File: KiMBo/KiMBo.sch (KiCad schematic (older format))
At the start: 74 parts, among them CON1 μSD, P1 BED, P10 CONN_01X02, P11 Serial, P12 μUSB, P13 USB_Type_A, P14 Ethernet, P15 JTAG, P16 CONN_01X04, P17 CONN_01X04, P18 CONN_01X04, P19 CONN_01X04, P2 ADC, P20 CONN_01X04, P21 CONN_01X04, P22 CONN_01X04, P23 CONN_01X04, P24 CONN_01X04, P25 BED_HEAT, P26 E_HEAT, P27 H_HEAT, P28 DOCK0_HEAT, P29 DOCK1_HEAT, P3 CONN_01X07, P30 E_FAN, P31 H_FAN, P32 PWM, P33 CASE_FAN, P34 HS_FAN, P4 CONN_01X07, P5 CONN_01X07, P6 CONN_01X07, P7 CONN_01X02, P8 CONN_01X02, P9 CONN_01X02, U1 MAX3370, X1 10118241-001RLF

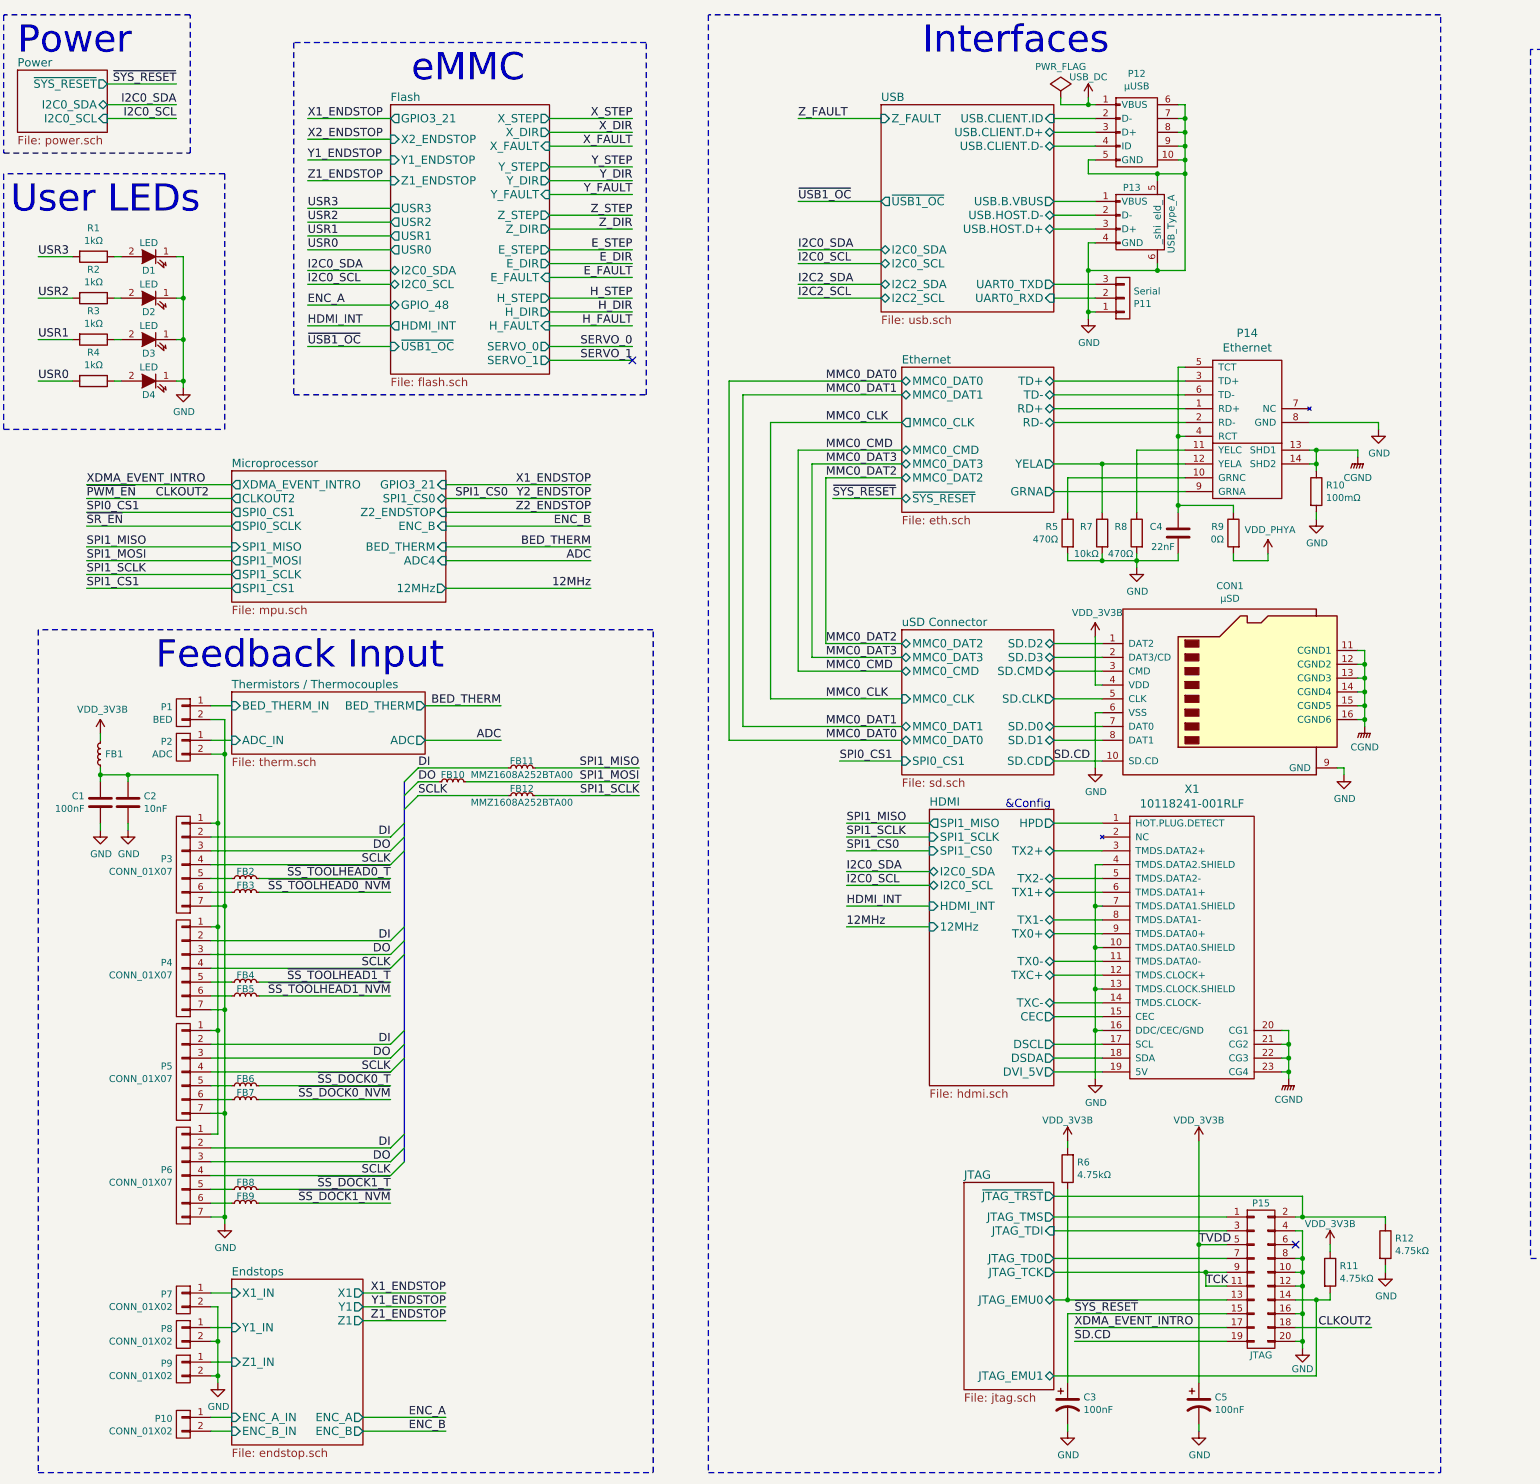
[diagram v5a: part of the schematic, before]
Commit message: Replace most electrolytic cap symbols symbols with the standard, non-polarized (ceramic) cap symbol
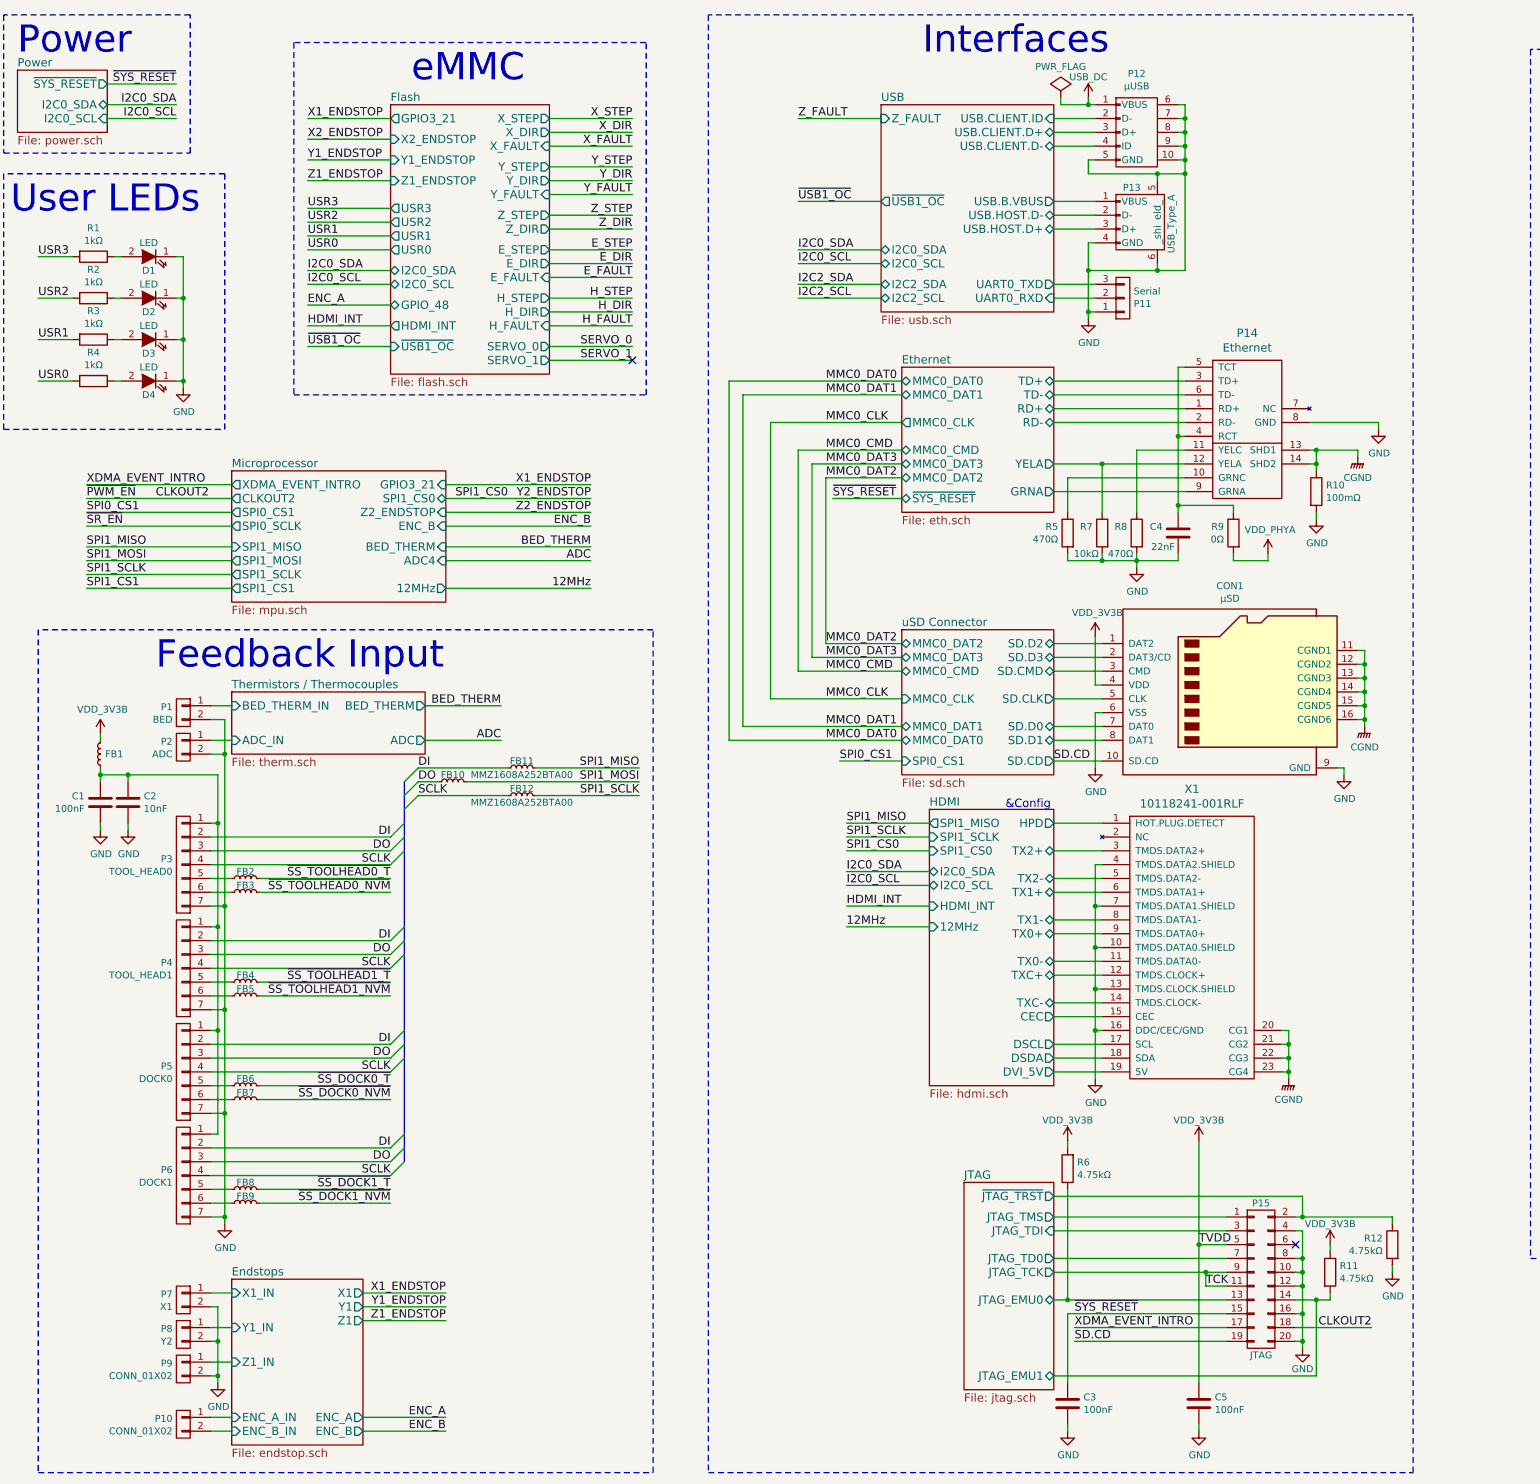
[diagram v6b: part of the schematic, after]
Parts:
- removed C3, C5: 100nF, symbol CP1
- added C3, C5: 100nF, symbol C
- C1, C2: footprint (none) -> Capacitors_SMD:C_0603
- P3: value CONN_01X07 -> TOOL_HEAD0
- P4: value CONN_01X07 -> TOOL_HEAD1
- P5: value CONN_01X07 -> DOCK0
- P6: value CONN_01X07 -> DOCK1
- P7: value CONN_01X02 -> X1
- P8: value CONN_01X02 -> Y2
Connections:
- net GND: now also C3.2, C5.2
- net VDD_3V3B: now also C5.1
- net ~SYS_RESET: now also C3.1
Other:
- moved on the sheet: R12
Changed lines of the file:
@@
 TVDD
-$Comp
-L CP1 C5
-U 1 1 58FEA321
-P 9250 10600
-F 0 "C5" H 9365 10646 50  0000 L CNN
-F 1 "100nF" H 9365 10555 50  0000 L CNN
-F 2 "" H 9250 10600 50  0001 C CNN
-F 3 "" H 9250 10600 50  0000 C CNN
-	1    9250 10600
-	1    0    0    -1
-$EndComp
 $Comp
 L GND #PWR011
@@
 $EndComp
 $Comp
-L CP1 C3
-U 1 1 58FEA335
-P 8300 10600
-F 0 "C3" H 8415 10646 50  0000 L CNN
-F 1 "100nF" H 8415 10555 50  0000 L CNN
-F 2 "" H 8300 10600 50  0001 C CNN
-F 3 "" H 8300 10600 50  0000 C CNN
-	1    8300 10600
-	1    0    0    -1
-$EndComp
-$Comp
 L GND #PWR012
 U 1 1 58FEA33C
@@
 L GND #PWR014
 U 1 1 58FEA383
-P 10600 9650
-F 0 "#PWR014" H 10600 9400 50  0001 C CNN
-F 1 "GND" H 10605 9477 50  0000 C CNN
-F 2 "" H 10600 9650 50  0000 C CNN
-F 3 "" H 10600 9650 50  0000 C CNN
-	1    10600 9650
+P 10650 9650
+F 0 "#PWR014" H 10650 9400 50  0001 C CNN
+F 1 "GND" H 10655 9477 50  0000 C CNN
+F 2 "" H 10650 9650 50  0000 C CNN
+F 3 "" H 10650 9650 50  0000 C CNN
+	1    10650 9650
 	1    0    0    -1
 $EndComp
@@
 L R R12
 U 1 1 58FEA389
-P 10600 9450
-F 0 "R12" H 10670 9496 50  0000 L CNN
-F 1 "4.75kΩ" H 10670 9405 50  0000 L CNN
-F 2 "" V 10530 9450 50  0001 C CNN
-F 3 "" H 10600 9450 50  0000 C CNN
-	1    10600 9450
-	1    0    0    -1
+P 10650 9450
+F 0 "R12" H 10720 9496 50  0000 L CNN
+F 1 "4.75kΩ" H 10720 9405 50  0000 L CNN
+F 2 "" V 10580 9450 50  0001 C CNN
+F 3 "" H 10650 9450 50  0000 C CNN
+	1    10650 9450
+	-1   0    0    -1
 $EndComp
 $Comp
@@
 P 1900 9850
 F 0 "P7" H 1978 9891 50  0000 L CNN
-F 1 "CONN_01X02" H 1978 9800 50  0000 L CNN
+F 1 "X1" H 1978 9800 50  0000 L CNN
 F 2 "" H 1900 9850 50  0001 C CNN
 F 3 "" H 1900 9850 50  0000 C CNN
@@
 P 1900 10100
 F 0 "P8" H 1978 10141 50  0000 L CNN
-F 1 "CONN_01X02" H 1978 10050 50  0000 L CNN
+F 1 "Y2" H 1978 10050 50  0000 L CNN
 F 2 "" H 1900 10100 50  0001 C CNN
 F 3 "" H 1900 10100 50  0000 C CNN
@@
 P 1900 6700
 F 0 "P3" H 1978 6741 50  0000 L CNN
-F 1 "CONN_01X07" H 1978 6650 50  0000 L CNN
+F 1 "TOOL_HEAD0" H 1978 6650 50  0000 L CNN
 F 2 "" H 1900 6700 50  0001 C CNN
 F 3 "" H 1900 6700 50  0000 C CNN
@@
 P 1900 8200
 F 0 "P5" H 1978 8241 50  0000 L CNN
-F 1 "CONN_01X07" H 1978 8150 50  0000 L CNN
+F 1 "DOCK0" H 1978 8150 50  0000 L CNN
 F 2 "" H 1900 8200 50  0001 C CNN
 F 3 "" H 1900 8200 50  0000 C CNN
@@
 P 1900 8950
 F 0 "P6" H 1978 8991 50  0000 L CNN
-F 1 "CONN_01X07" H 1978 8900 50  0000 L CNN
+F 1 "DOCK1" H 1978 8900 50  0000 L CNN
 F 2 "" H 1900 8950 50  0001 C CNN
 F 3 "" H 1900 8950 50  0000 C CNN
@@
 P 1900 7450
 F 0 "P4" H 1978 7491 50  0000 L CNN
-F 1 "CONN_01X07" H 1978 7400 50  0000 L CNN
+F 1 "TOOL_HEAD1" H 1978 7400 50  0000 L CNN
 F 2 "" H 1900 7450 50  0001 C CNN
 F 3 "" H 1900 7450 50  0000 C CNN
@@
 F 0 "C2" H 1614 6296 50  0000 L CNN
 F 1 "10nF" H 1614 6205 50  0000 L CNN
-F 2 "" H 1538 6100 50  0001 C CNN
+F 2 "Capacitors_SMD:C_0603" H 1538 6100 50  0001 C CNN
 F 3 "" H 1500 6250 50  0000 C CNN
 	1    1500 6250
@@
 F 0 "C1" H 1415 6296 50  0000 L CNN
 F 1 "100nF" H 1415 6205 50  0000 L CNN
-F 2 "" H 1338 6100 50  0001 C CNN
+F 2 "Capacitors_SMD:C_0603" H 1338 6100 50  0001 C CNN
 F 3 "" H 1300 6250 50  0000 C CNN
 	1    1300 6250
@@
 	9450 10150 8350 10150
 Wire Wire Line
-	9950 9250 10600 9250
+	9950 9250 10650 9250
 Wire Wire Line
 	9450 9750 9300 9750
@@
 	10200 9850 10200 9800
 Wire Wire Line
-	10600 9250 10600 9300
-Wire Wire Line
-	10600 9650 10600 9600
+	10650 9250 10650 9300
+Wire Wire Line
+	10650 9650 10650 9600
 Wire Wire Line
 	8500 6700 8500 8250
@@
 	5700 550  5700 11100
 Wire Notes Line
-	5700 11100 11000 11100
-Wire Notes Line
-	11000 11100 11000 550
-Wire Notes Line
-	11000 550  5700 550
+	5700 11100 10800 11100
+Wire Notes Line
+	10800 11100 10800 550
+Wire Notes Line
+	10800 550  5700 550
 Wire Notes Line
 	850  11100 5300 11100
@@
 Wire Wire Line
 	8300 9950 8300 10450
+$Comp
+L C C3
+U 1 1 58E7EB04
+P 8300 10600
+F 0 "C3" H 8415 10646 50  0000 L CNN
+F 1 "100nF" H 8415 10555 50  0000 L CNN
+F 2 "" H 8338 10450 50  0000 C CNN
+F 3 "" H 8300 10600 50  0000 C CNN
+	1    8300 10600
+	1    0    0    -1
+$EndComp
+$Comp
+L C C5
+U 1 1 58E8038E
+P 9250 10600
+F 0 "C5" H 9365 10646 50  0000 L CNN
+F 1 "100nF" H 9365 10555 50  0000 L CNN
+F 2 "" H 9288 10450 50  0000 C CNN
+F 3 "" H 9250 10600 50  0000 C CNN
+	1    9250 10600
+	1    0    0    -1
+$EndComp
 $EndSCHEMATC

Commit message: Rename connectors to their respective functionality
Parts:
- P1: value BED -> BED_THERM
- P10: value CONN_01X02 -> ENC
- P16: value CONN_01X04 -> E_MOTOR
- P17: value CONN_01X04 -> H_MOTOR
- P18: value CONN_01X04 -> X0_MOTOR
- P19: value CONN_01X04 -> X1_MOTOR
- P20: value CONN_01X04 -> Y0_MOTOR
- P21: value CONN_01X04 -> Y1_MOTOR
- P22: value CONN_01X04 -> Z0_MOTOR
- P23: value CONN_01X04 -> Z1_MOTOR
- P24: value CONN_01X04 -> Z2_MOTOR
- P3: value TOOL_HEAD0 -> TOOLHEAD0
- P4: value TOOL_HEAD1 -> TOOLHEAD1
- P9: value CONN_01X02 -> Z1
- X1: value 10118241-001RLF -> HDMI
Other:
- note added: "EPM/Servo"
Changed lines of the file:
@@
 P 1900 5600
 F 0 "P1" H 1978 5641 50  0000 L CNN
-F 1 "BED" H 1978 5550 50  0000 L CNN
+F 1 "BED_THERM" H 1978 5550 50  0000 L CNN
 F 2 "" H 1900 5600 50  0001 C CNN
 F 3 "" H 1900 5600 50  0000 C CNN
@@
 P 15000 2900
 F 0 "P16" H 15078 2941 50  0000 L CNN
-F 1 "CONN_01X04" H 15078 2850 50  0000 L CNN
+F 1 "E_MOTOR" H 15078 2850 50  0000 L CNN
 F 2 "" H 15000 2900 50  0001 C CNN
 F 3 "" H 15000 2900 50  0000 C CNN
@@
 P 15000 3350
 F 0 "P17" H 15078 3391 50  0000 L CNN
-F 1 "CONN_01X04" H 15078 3300 50  0000 L CNN
+F 1 "H_MOTOR" H 15078 3300 50  0000 L CNN
 F 2 "" H 15000 3350 50  0001 C CNN
 F 3 "" H 15000 3350 50  0000 C CNN
@@
 P 15000 3800
 F 0 "P18" H 15078 3841 50  0000 L CNN
-F 1 "CONN_01X04" H 15078 3750 50  0000 L CNN
+F 1 "X0_MOTOR" H 15078 3750 50  0000 L CNN
 F 2 "" H 15000 3800 50  0001 C CNN
 F 3 "" H 15000 3800 50  0000 C CNN
@@
 P 15000 4250
 F 0 "P19" H 15078 4291 50  0000 L CNN
-F 1 "CONN_01X04" H 15078 4200 50  0000 L CNN
+F 1 "X1_MOTOR" H 15078 4200 50  0000 L CNN
 F 2 "" H 15000 4250 50  0001 C CNN
 F 3 "" H 15000 4250 50  0000 C CNN
@@
 P 15000 5100
 F 0 "P21" H 15078 5141 50  0000 L CNN
-F 1 "CONN_01X04" H 15078 5050 50  0000 L CNN
+F 1 "Y1_MOTOR" H 15078 5050 50  0000 L CNN
 F 2 "" H 15000 5100 50  0001 C CNN
 F 3 "" H 15000 5100 50  0000 C CNN
@@
 P 9200 7300
 F 0 "X1" H 9200 8447 60  0000 C CNN
-F 1 "10118241-001RLF" H 9200 8341 60  0000 C CNN
+F 1 "HDMI" H 9200 8341 60  0000 C CNN
 F 2 "" H 9250 7450 60  0001 C CNN
-F 3 "" H 9250 7450 60  0001 C CNN
+F 3 "http://media.digikey.com/pdf/Data%20Sheets/FCI%20PDFs/10118241-001RLF_Webpage.PDF" H 9250 7450 60  0001 C CNN
 	1    9200 7300
 	1    0    0    -1
@@
 P 1900 10350
 F 0 "P9" H 1978 10391 50  0000 L CNN
-F 1 "CONN_01X02" H 1978 10300 50  0000 L CNN
+F 1 "Z1" H 1978 10300 50  0000 L CNN
 F 2 "" H 1900 10350 50  0001 C CNN
 F 3 "" H 1900 10350 50  0000 C CNN
@@
 P 15000 5550
 F 0 "P22" H 15078 5591 50  0000 L CNN
-F 1 "CONN_01X04" H 15078 5500 50  0000 L CNN
+F 1 "Z0_MOTOR" H 15078 5500 50  0000 L CNN
 F 2 "" H 15000 5550 50  0001 C CNN
 F 3 "" H 15000 5550 50  0000 C CNN
@@
 P 1900 10750
 F 0 "P10" H 1978 10791 50  0000 L CNN
-F 1 "CONN_01X02" H 1978 10700 50  0000 L CNN
+F 1 "ENC" H 1978 10700 50  0000 L CNN
 F 2 "" H 1900 10750 50  0001 C CNN
 F 3 "" H 1900 10750 50  0000 C CNN
@@
 P 1900 6700
 F 0 "P3" H 1978 6741 50  0000 L CNN
-F 1 "TOOL_HEAD0" H 1978 6650 50  0000 L CNN
+F 1 "TOOLHEAD0" H 1978 6650 50  0000 L CNN
 F 2 "" H 1900 6700 50  0001 C CNN
 F 3 "" H 1900 6700 50  0000 C CNN
@@
 P 15000 6000
 F 0 "P23" H 15078 6041 50  0000 L CNN
-F 1 "CONN_01X04" H 15078 5950 50  0000 L CNN
+F 1 "Z1_MOTOR" H 15078 5950 50  0000 L CNN
 F 2 "" H 15000 6000 50  0001 C CNN
 F 3 "" H 15000 6000 50  0000 C CNN
@@
 P 15000 6450
 F 0 "P24" H 15078 6491 50  0000 L CNN
-F 1 "CONN_01X04" H 15078 6400 50  0000 L CNN
+F 1 "Z2_MOTOR" H 15078 6400 50  0000 L CNN
 F 2 "" H 15000 6450 50  0001 C CNN
 F 3 "" H 15000 6450 50  0000 C CNN
@@
 P 1900 7450
 F 0 "P4" H 1978 7491 50  0000 L CNN
-F 1 "TOOL_HEAD1" H 1978 7400 50  0000 L CNN
+F 1 "TOOLHEAD1" H 1978 7400 50  0000 L CNN
 F 2 "" H 1900 7450 50  0001 C CNN
 F 3 "" H 1900 7450 50  0000 C CNN
@@
 P 15000 4700
 F 0 "P20" H 15078 4741 50  0000 L CNN
-F 1 "CONN_01X04" H 15078 4650 50  0000 L CNN
+F 1 "Y0_MOTOR" H 15078 4650 50  0000 L CNN
 F 2 "" H 15000 4700 50  0001 C CNN
 F 3 "" H 15000 4700 50  0000 C CNN
@@
 	1    0    0    -1
 $EndComp
+Text Notes 14800 1700 0    60   ~ 0
+EPM/Servo
 $EndSCHEMATC
